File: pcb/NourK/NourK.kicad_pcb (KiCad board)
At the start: 2 copper layers, 218 parts, among them IC1 IS31FL3733B-QFLS4-TR, IC2 IS31FL3733B-QFLS4-TR, J1 SJ-435107RS, J2 USB_C_Receptacle_USB2.0, J3 Conn_ARM_JTAG_SWD_10, J4 SJ-435107RS, J5 USB_C_Receptacle_USB2.0, J6 Conn_ARM_JTAG_SWD_10, SW1 SW_SPST_G, SW10 LAYER, SW11 I, SW12 K, SW13 ,, SW14 LAYER, SW15 O, SW16 L, SW17 ., SW18 LAYER, SW19 P, SW2 SW_SPST_G, SW20 ;, SW21 /, SW22 RCTRL, SW23 [, SW24 ', SW25 RSHIFT, SW26 ], SW27 ENTER, SW28 SW_SPST_G, SW29 SW_SPST_G, SW3 Y, SW30 ESCAPE, SW31 OSKEY, SW32 TAB, SW33 GRAVE, SW34 LEFT_SHIFT, SW35 Q, SW36 A, SW37 Z, SW38 LEFT_CTRL, SW39 W, SW4 H, SW40 S, SW41 X, SW42 LAYER1, SW43 E, SW44 D, SW45 C, SW46 LAYER2, SW47 R, SW48 F, SW49 V, SW5 N, SW50 LEFT_ALT, SW51 T, SW52 G, SW53 B, SW54 SPACE, SW6 SPACE, SW7 U, SW8 J, SW9 M, U1 STM32L082CZYx, U2 AP2112K-3.3, U3 STM32L082CZYx, U4 AP2112K-3.3, Y1 8MHz, Y2 32.768KHz, Y3 8MHz, Y4 32.768KHz

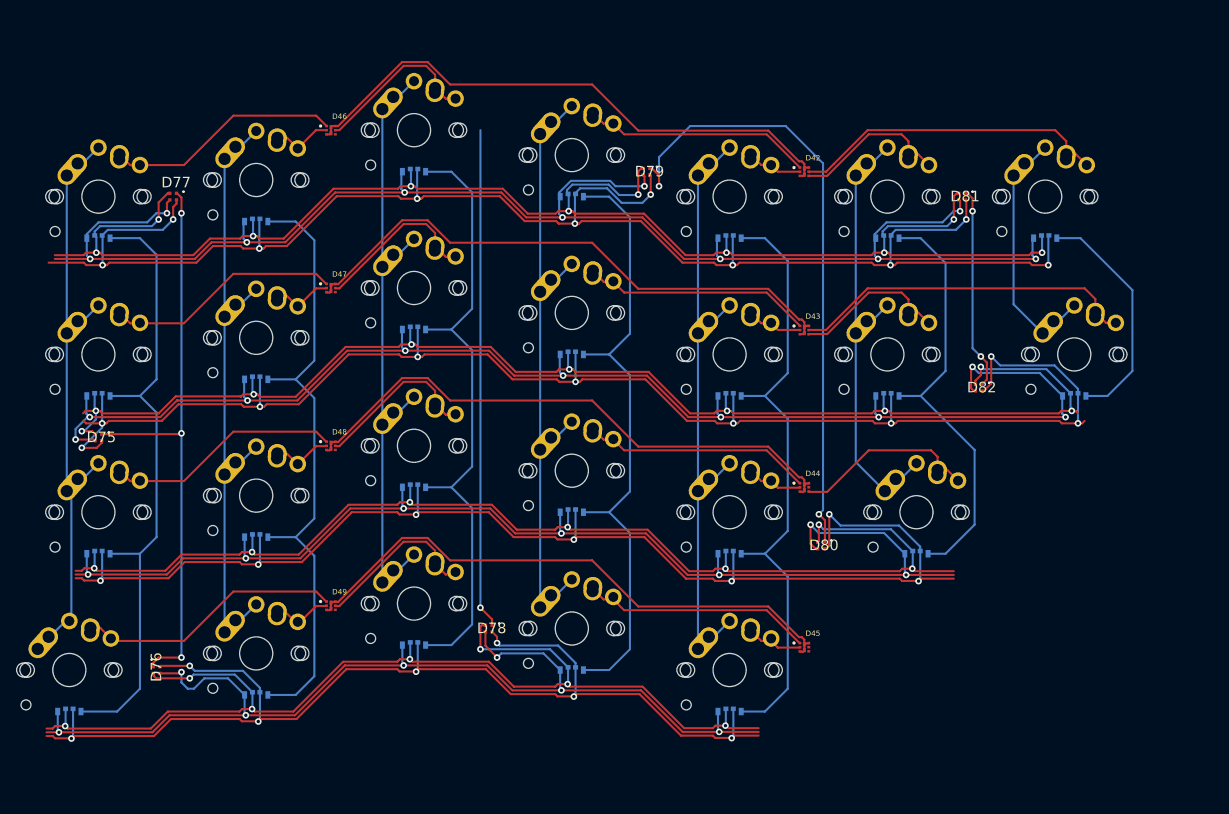
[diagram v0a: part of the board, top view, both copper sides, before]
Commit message: Matrices connection traces
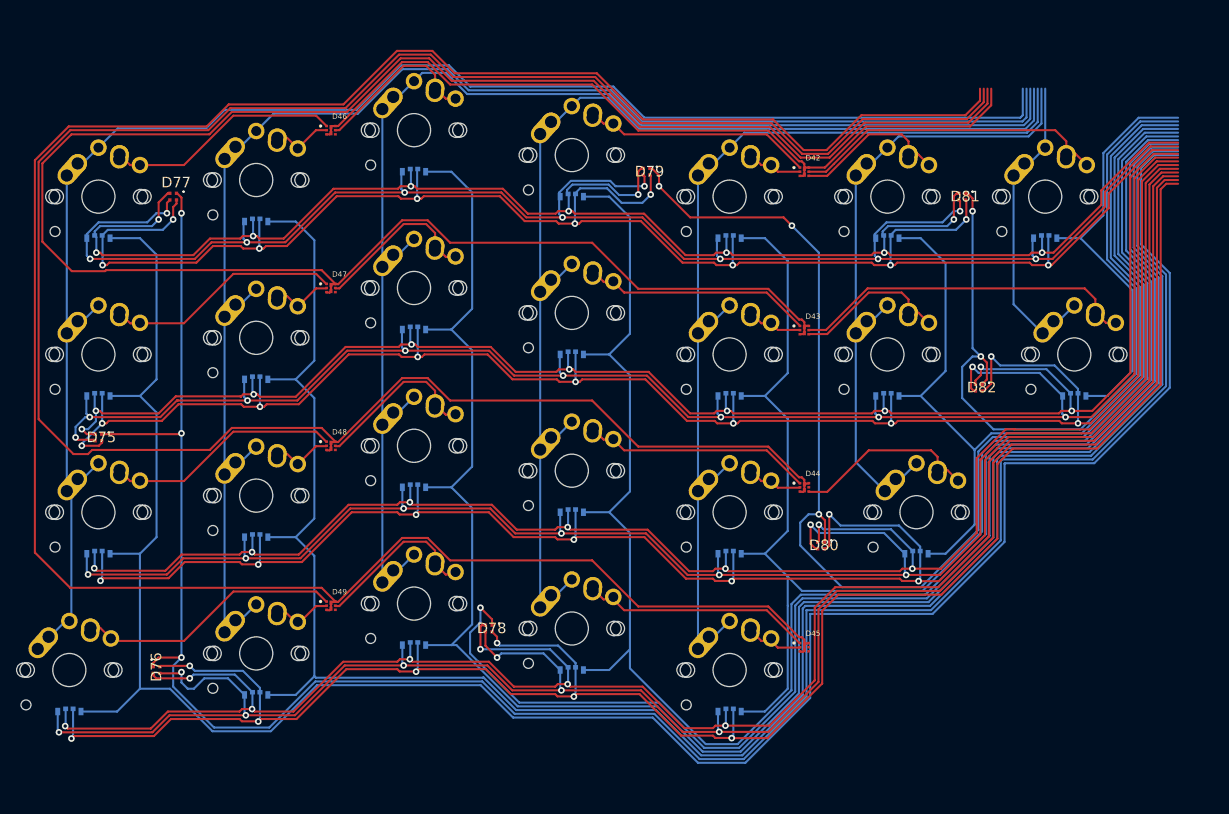
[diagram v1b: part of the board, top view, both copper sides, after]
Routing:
- net /lhs/LHS Core/KEY.ROW4: track 69.1 -> 283.1 mm
- net /lhs/LHS Core/KEY.ROW3: track 69.1 -> 267.8 mm
- net /lhs/LHS Core/LED.CS_COL8: track 70.0 -> 265.5 mm
- net /lhs/LHS Core/LED.CS_COL7: track 76.6 -> 272.0 mm
- net /lhs/LHS Core/KEY.ROW2: track 69.1 -> 244.5 mm
- net /lhs/LHS Core/LED.CS_COL6: track 76.0 -> 246.3 mm
- net /lhs/LHS Core/LED.CS_COL5: track 75.6 -> 230.8 mm
- net /lhs/LHS Core/LED.CS_COL4: track 75.6 -> 210.1 mm
- net /lhs/LHS Core/KEY.COL7: track 68.8 -> 190.1 mm
- net /lhs/LHS Core/KEY.COL6: track 77.8 -> 179.9 mm
- net /lhs/LHS Core/LED.CS_COL9: track 60.2 -> 161.0 mm
- net /lhs/LHS Core/LED.SW_RED4: track 130.7 -> 231.4 mm
- net /lhs/LHS Core/LED.SW_GREEN4: track 132.4 -> 232.0 mm
- net /lhs/LHS Core/LED.SW_BLUE4: track 138.2 -> 237.3 mm
- net /lhs/LHS Core/LED.CS_COL3: track 75.2 -> 171.7 mm
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
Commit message: Initial tracing of the keyboard controller
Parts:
- moved SW29 110.0 mm to (315.7, -18.8)
- moved C36 100.4 mm to (323.4, -2.60), turned to 180 degrees
- moved R24 98.7 mm to (313.8, -13.0)
- moved SW28 90.3 mm to (323.5, 3.25)
- moved R20 87.7 mm to (323.4, 9.00), turned to 180 degrees
- moved J5 80.1 mm to (294.2, -9.75), turned to 180 degrees
- moved Y3 76.2 mm to (301.5, 41.0)
- moved C38 75.4 mm to (306.8, 42.2)
- moved R17 71.7 mm to (301.8, -8.00)
- moved J6 69.0 mm to (313.2, 18.9)
- moved C33 62.9 mm to (292.5, 21.8)
- moved C32 58.3 mm to (289.8, 15.0), turned to -90 degrees
- moved J1 55.8 mm to (237.8, 6.90)
- moved C35 55.1 mm to (286.2, -3.33), turned to 180 degrees
- moved R16 53.3 mm to (301.8, -5.80)
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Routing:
- net GND: track 0.00 -> 83.2 mm, vias 0 -> 10
- net VCC: track 0.00 -> 29.6 mm
- net VBUS: track 0.00 -> 25.7 mm
- net /lhs/LHS Core/~{RST}: track 0.00 -> 11.6 mm
- net Net-(J5-PadB5): track 0.00 -> 9.56 mm, vias 0 -> 2
- net Net-(J5-PadA5): track 0.00 -> 8.99 mm
- net /lhs/LHS Core/BOOT0: track 0.00 -> 8.39 mm
- net Net-(C38-Pad1): track 0.00 -> 4.68 mm
- net Net-(IC2-Pad47): track 0.00 -> 4.46 mm
- net Net-(IC2-Pad46): track 0.00 -> 3.52 mm
- net Net-(IC2-Pad35): track 0.00 -> 3.34 mm
- net /lhs/LHS Core/OSC32_IN: track 0.00 -> 2.91 mm
- net /lhs/LHS Core/OSC32_OUT: track 0.00 -> 2.89 mm
- net /lhs/LHS Core/OSC_IN: track 0.00 -> 2.71 mm
- net +3V3: track 0.00 -> 1.90 mm
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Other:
- copper layers 2 -> 6

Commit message: Re-traced RHS
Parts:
- removed C21, C22, C24, C26: 0.47uF, Capacitor_SMD:C_0805_2012Metric
- removed C23, C25, C27: 0.1uF, Capacitor_SMD:C_0805_2012Metric
- removed C28, C29, C31, C34: 100uF, Capacitor_SMD:C_0805_2012Metric
- removed C30, C33, C35: 1uF, Capacitor_SMD:C_0805_2012Metric
- removed C32: 10uF, Capacitor_SMD:C_0805_2012Metric
- removed C36: 10nF, Capacitor_SMD:C_0805_2012Metric
- removed C37, C38: 10pF, Capacitor_SMD:C_0805_2012Metric
- removed C39, C40: 7pF, Capacitor_SMD:C_0805_2012Metric
- removed FB2: FerriteBead, Resistor_SMD:R_0805_2012Metric
- removed IC2: IS31FL3733B-QFLS4-TR, Nour_KB:QFN40P600X600X80-49N-D
- removed J4: SJ-435107RS, Nour_KB:CUI_SJ-435107RS
- removed J5: USB_C_Receptacle_USB2.0, Nour_KB:GCT_USB4085-GF-A_REVA4
- removed J6: Conn_ARM_JTAG_SWD_10, Connector_PinSocket_1.27mm:PinSocket_2x05_P1.27mm_Vertical
- removed R13, R14, R20, R24: 100K, Resistor_SMD:R_0805_2012Metric
- removed R15: R, Resistor_SMD:R_0805_2012Metric
- removed R16, R17: 5K1, Resistor_SMD:R_0805_2012Metric
- removed R18, R19: 4k7, Resistor_SMD:R_0805_2012Metric
- removed R21, R22: 10K, Resistor_SMD:R_0805_2012Metric
- removed R23: 1990, Resistor_SMD:R_0805_2012Metric
- removed SW28, SW29: SW_SPST_G, Nour_KB:EVQP9102W
- removed Y3: 8MHz, Nour_KB:ECS801830BAGNTR
- removed Y4: 32.768KHz, Nour_KB:ECS327712TR
- added D83: LED_UG_4_2, Nour_KB:LTRBR37G4R4S012502R18, F.Cu at (137.5, 176.0)
- added D84: LED_UG_3_3, Nour_KB:LTRBR37G4R4S012502R18, F.Cu at (137.5, 227.5)
- added U5: NourK_Core, Nour_KB:NourKB_Core, F.Cu at (149.4, 86.4)
- C1, C2, C6: value 0.47uF -> 100uF
- C10: value 1uF -> 7pF
- C11: value 100uF -> 7pF
- C12: value 10uF -> 10pF
- C13: value 1uF -> 10pF
- C14: value 100uF -> 0.47uF
- C15: value 1uF -> 0.47uF
- C16: value 10nF -> 0.1uF
- C17: value 10pF -> 0.47uF
- C18: value 10pF -> 0.1uF
- C19: value 7pF -> 0.47uF
- C20: value 7pF -> 0.1uF
- C3: value 0.1uF -> 100uF
- C4: value 0.47uF -> 10uF
- C5, C7: value 0.1uF -> 1uF
- C8: value 100uF -> 1uF
- C9: value 100uF -> 10nF
- J2: value USB_C_Receptacle_USB2.0 -> Conn_ARM_JTAG_SWD_10; footprint Nour_KB:GCT_USB4085-GF-A_REVA4 -> Connector_PinSocket_1.27mm:PinSocket_2x05_P1.27mm_Vertical
- J3: value Conn_ARM_JTAG_SWD_10 -> USB_C_Receptacle_USB2.0; footprint Connector_PinSocket_1.27mm:PinSocket_2x05_P1.27mm_Vertical -> Nour_KB:GCT_USB4085-GF-A_REVA4
- R1: value 100K -> 10K
- R10, R9: value 10K -> 5K1
- R11: value 1990 -> 100K
- R12: value 100K -> R
- R2: value 100K -> 4k7
- R3: value R -> 4k7
- R4: value 5K1 -> 100K
- R5: value 5K1 -> 10K
- R6: value 4k7 -> 100K
- R7: value 4k7 -> 1990
- U3: value STM32L082CZYx -> NourK_Core; footprint Package_CSP:ST_WLCSP-49_Die447 -> Nour_KB:NourKB_Core_2
- U4: value AP2112K-3.3 -> NourK_Core; footprint Package_TO_SOT_SMD:SOT-23-5 -> Nour_KB:NourKB_Core
- Y1: value 8MHz -> 32.768KHz; footprint Nour_KB:ECS801830BAGNTR -> Nour_KB:ECS327712TR
- Y2: value 32.768KHz -> 8MHz; footprint Nour_KB:ECS327712TR -> Nour_KB:ECS801830BAGNTR
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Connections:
- net /lhs/LHS Core/LED.CS_COL1 renamed /lhs/LHS LEDs/LED.CS_COL1
- net /lhs/LHS Core/LED.CS_COL10 renamed /lhs/LHS LEDs/LED.CS_COL10
- net /lhs/LHS Core/LED.CS_COL11 renamed /lhs/LHS LEDs/LED.CS_COL11
- net /lhs/LHS Core/LED.CS_COL2 renamed /lhs/LHS LEDs/LED.CS_COL2
- net /lhs/LHS Core/LED.CS_COL3 renamed /lhs/LHS LEDs/LED.CS_COL3
- net /lhs/LHS Core/LED.CS_COL4 renamed /lhs/LHS LEDs/LED.CS_COL4
- net /lhs/LHS Core/LED.CS_COL5 renamed /lhs/LHS LEDs/LED.CS_COL5
- net /lhs/LHS Core/LED.CS_COL6 renamed /lhs/LHS LEDs/LED.CS_COL6
- net /lhs/LHS Core/LED.CS_COL7 renamed /lhs/LHS LEDs/LED.CS_COL7
- net /lhs/LHS Core/LED.CS_COL8 renamed /lhs/LHS LEDs/LED.CS_COL8
- net /lhs/LHS Core/LED.SW_BLUE1 renamed /lhs/LHS LEDs/LED.SW_BLUE1
- net /lhs/LHS Core/LED.SW_BLUE2 renamed /lhs/LHS LEDs/LED.SW_BLUE2
- net /lhs/LHS Core/LED.SW_BLUE3 renamed /lhs/LHS LEDs/LED.SW_BLUE3
- net /lhs/LHS Core/LED.SW_BLUE4 renamed /lhs/LHS LEDs/LED.SW_BLUE4
- net /lhs/LHS Core/LED.SW_GREEN1 renamed /lhs/LHS LEDs/LED.SW_GREEN1
- net /lhs/LHS Core/LED.SW_GREEN2 renamed /lhs/LHS LEDs/LED.SW_GREEN2
- net /lhs/LHS Core/LED.SW_GREEN3 renamed /lhs/LHS LEDs/LED.SW_GREEN3
- net /lhs/LHS Core/LED.SW_GREEN4 renamed /lhs/LHS LEDs/LED.SW_GREEN4
- net /lhs/LHS Core/LED.SW_RED1 renamed /lhs/LHS LEDs/LED.SW_RED1
- net /lhs/LHS Core/LED.SW_RED2 renamed /lhs/LHS LEDs/LED.SW_RED2
- net /lhs/LHS Core/LED.SW_RED3 renamed /lhs/LHS LEDs/LED.SW_RED3
- net /lhs/LHS Core/LED.SW_RED4 renamed /lhs/LHS LEDs/LED.SW_RED4
- C10 pad 1: VBUS -> /core/OSC32_IN
- C11 pad 1: VCC -> /core/OSC32_OUT
- C12 pad 1: VCC -> /core/OSC_IN
- C13 pad 1: /rhs/RHS Core/VDDA -> Net-(C13-Pad1)
- C14 pad 1: /rhs/RHS Core/VDDA -> VCC
- C15 pad 1: +3V3 -> VCC
- C16 pad 1: /rhs/RHS Core/~{RST} -> VCC
- C17 pad 1: /rhs/RHS Core/OSC_IN -> VCC
- C18 pad 1: Net-(C18-Pad1) -> VCC
- C19 pad 1: /rhs/RHS Core/OSC32_IN -> VCC
- C20 pad 1: /rhs/RHS Core/OSC32_OUT -> VCC
- C5 pad 1: VCC -> /core/VDDA
- C6 pad 1: VCC -> /core/VDDA
- C7 pad 1: VCC -> VBUS
- C9 pad 1: VCC -> /core/~{RST}
- D1 pad 3: /rhs/RHS Core/KEY.ROW1 -> /rhs/RHS Keys/KEY.ROW10
- D1 pad 6: /rhs/RHS Core/KEY.ROW1 -> /rhs/RHS Keys/KEY.ROW10
- D1 pad 7: /rhs/RHS Core/KEY.ROW1 -> /rhs/RHS Keys/KEY.ROW10
- D1 pad 8: /rhs/RHS Core/KEY.ROW1 -> /rhs/RHS Keys/KEY.ROW10
- D10 pad 1: /rhs/RHS Core/LED.CS_COL1 -> /rhs/RHS LEDs/LED.CS_COL12
- D10 pad 2: /rhs/RHS Core/LED.SW_BLUE2 -> /rhs/RHS LEDs/LED.SW_BLUE3
- D10 pad 3: /rhs/RHS Core/LED.SW_GREEN2 -> /rhs/RHS LEDs/LED.SW_GREEN3
- D10 pad 4: /rhs/RHS Core/LED.SW_RED2 -> /rhs/RHS LEDs/LED.SW_RED3
- D11 pad 1: /rhs/RHS Core/LED.CS_COL1 -> /rhs/RHS LEDs/LED.CS_COL12
- D11 pad 2: /rhs/RHS Core/LED.SW_BLUE3 -> /rhs/RHS LEDs/LED.SW_BLUE2
- D11 pad 3: /rhs/RHS Core/LED.SW_GREEN3 -> /rhs/RHS LEDs/LED.SW_GREEN2
- D11 pad 4: /rhs/RHS Core/LED.SW_RED3 -> /rhs/RHS LEDs/LED.SW_RED2
- D12 pad 1: /rhs/RHS Core/LED.CS_COL1 -> /rhs/RHS LEDs/LED.CS_COL12
- D12 pad 2: /rhs/RHS Core/LED.SW_BLUE4 -> /rhs/RHS LEDs/LED.SW_BLUE1
- D12 pad 3: /rhs/RHS Core/LED.SW_GREEN4 -> /rhs/RHS LEDs/LED.SW_GREEN1
- D12 pad 4: /rhs/RHS Core/LED.SW_RED4 -> /rhs/RHS LEDs/LED.SW_RED1
- D13 pad 1: /rhs/RHS Core/LED.CS_COL2 -> /rhs/RHS LEDs/LED.CS_COL11
- D13 pad 2: /rhs/RHS Core/LED.SW_BLUE1 -> /rhs/RHS LEDs/LED.SW_BLUE4
- D13 pad 3: /rhs/RHS Core/LED.SW_GREEN1 -> /rhs/RHS LEDs/LED.SW_GREEN4
- D13 pad 4: /rhs/RHS Core/LED.SW_RED1 -> /rhs/RHS LEDs/LED.SW_RED4
- D14 pad 1: /rhs/RHS Core/LED.CS_COL2 -> /rhs/RHS LEDs/LED.CS_COL11
- D14 pad 2: /rhs/RHS Core/LED.SW_BLUE2 -> /rhs/RHS LEDs/LED.SW_BLUE3
- D14 pad 3: /rhs/RHS Core/LED.SW_GREEN2 -> /rhs/RHS LEDs/LED.SW_GREEN3
- D14 pad 4: /rhs/RHS Core/LED.SW_RED2 -> /rhs/RHS LEDs/LED.SW_RED3
- D15 pad 1: /rhs/RHS Core/LED.CS_COL2 -> /rhs/RHS LEDs/LED.CS_COL11
- D15 pad 2: /rhs/RHS Core/LED.SW_BLUE3 -> /rhs/RHS LEDs/LED.SW_BLUE2
- D15 pad 3: /rhs/RHS Core/LED.SW_GREEN3 -> /rhs/RHS LEDs/LED.SW_GREEN2
- D15 pad 4: /rhs/RHS Core/LED.SW_RED3 -> /rhs/RHS LEDs/LED.SW_RED2
- D16 pad 1: /rhs/RHS Core/LED.CS_COL2 -> /rhs/RHS LEDs/LED.CS_COL11
- D16 pad 2: /rhs/RHS Core/LED.SW_BLUE4 -> /rhs/RHS LEDs/LED.SW_BLUE1
- D16 pad 3: /rhs/RHS Core/LED.SW_GREEN4 -> /rhs/RHS LEDs/LED.SW_GREEN1
- D16 pad 4: /rhs/RHS Core/LED.SW_RED4 -> /rhs/RHS LEDs/LED.SW_RED1
- D17 pad 1: /rhs/RHS Core/LED.CS_COL3 -> /rhs/RHS LEDs/LED.CS_COL10
- D17 pad 2: /rhs/RHS Core/LED.SW_BLUE1 -> /rhs/RHS LEDs/LED.SW_BLUE4
- D17 pad 3: /rhs/RHS Core/LED.SW_GREEN1 -> /rhs/RHS LEDs/LED.SW_GREEN4
- D17 pad 4: /rhs/RHS Core/LED.SW_RED1 -> /rhs/RHS LEDs/LED.SW_RED4
- D18 pad 1: /rhs/RHS Core/LED.CS_COL3 -> /rhs/RHS LEDs/LED.CS_COL10
- D18 pad 2: /rhs/RHS Core/LED.SW_BLUE2 -> /rhs/RHS LEDs/LED.SW_BLUE3
- D18 pad 3: /rhs/RHS Core/LED.SW_GREEN2 -> /rhs/RHS LEDs/LED.SW_GREEN3
- D18 pad 4: /rhs/RHS Core/LED.SW_RED2 -> /rhs/RHS LEDs/LED.SW_RED3
- D19 pad 1: /rhs/RHS Core/LED.CS_COL3 -> /rhs/RHS LEDs/LED.CS_COL10
- D19 pad 2: /rhs/RHS Core/LED.SW_BLUE3 -> /rhs/RHS LEDs/LED.SW_BLUE2
- D19 pad 3: /rhs/RHS Core/LED.SW_GREEN3 -> /rhs/RHS LEDs/LED.SW_GREEN2
- D19 pad 4: /rhs/RHS Core/LED.SW_RED3 -> /rhs/RHS LEDs/LED.SW_RED2
- D2 pad 3: /rhs/RHS Core/KEY.ROW2 -> /rhs/RHS Keys/KEY.ROW9
- D2 pad 6: /rhs/RHS Core/KEY.ROW2 -> /rhs/RHS Keys/KEY.ROW9
- D2 pad 7: /rhs/RHS Core/KEY.ROW2 -> /rhs/RHS Keys/KEY.ROW9
- D2 pad 8: /rhs/RHS Core/KEY.ROW2 -> /rhs/RHS Keys/KEY.ROW9
- D20 pad 1: /rhs/RHS Core/LED.CS_COL3 -> /rhs/RHS LEDs/LED.CS_COL10
- D20 pad 2: /rhs/RHS Core/LED.SW_BLUE4 -> /rhs/RHS LEDs/LED.SW_BLUE1
- D20 pad 3: /rhs/RHS Core/LED.SW_GREEN4 -> /rhs/RHS LEDs/LED.SW_GREEN1
- D20 pad 4: /rhs/RHS Core/LED.SW_RED4 -> /rhs/RHS LEDs/LED.SW_RED1
- D21 pad 1: /rhs/RHS Core/LED.CS_COL4 -> /rhs/RHS LEDs/LED.CS_COL9
- D21 pad 2: /rhs/RHS Core/LED.SW_BLUE1 -> /rhs/RHS LEDs/LED.SW_BLUE4
- D21 pad 3: /rhs/RHS Core/LED.SW_GREEN1 -> /rhs/RHS LEDs/LED.SW_GREEN4
- D21 pad 4: /rhs/RHS Core/LED.SW_RED1 -> /rhs/RHS LEDs/LED.SW_RED4
- D22 pad 1: /rhs/RHS Core/LED.CS_COL4 -> /rhs/RHS LEDs/LED.CS_COL9
- D22 pad 2: /rhs/RHS Core/LED.SW_BLUE2 -> /rhs/RHS LEDs/LED.SW_BLUE3
- D22 pad 3: /rhs/RHS Core/LED.SW_GREEN2 -> /rhs/RHS LEDs/LED.SW_GREEN3
- D22 pad 4: /rhs/RHS Core/LED.SW_RED2 -> /rhs/RHS LEDs/LED.SW_RED3
- D23 pad 1: /rhs/RHS Core/LED.CS_COL4 -> /rhs/RHS LEDs/LED.CS_COL9
- D23 pad 2: /rhs/RHS Core/LED.SW_BLUE3 -> /rhs/RHS LEDs/LED.SW_BLUE2
- D23 pad 3: /rhs/RHS Core/LED.SW_GREEN3 -> /rhs/RHS LEDs/LED.SW_GREEN2
- D23 pad 4: /rhs/RHS Core/LED.SW_RED3 -> /rhs/RHS LEDs/LED.SW_RED2
- D24 pad 1: /rhs/RHS Core/LED.CS_COL4 -> /rhs/RHS LEDs/LED.CS_COL9
- D24 pad 2: /rhs/RHS Core/LED.SW_BLUE4 -> /rhs/RHS LEDs/LED.SW_BLUE1
- D24 pad 3: /rhs/RHS Core/LED.SW_GREEN4 -> /rhs/RHS LEDs/LED.SW_GREEN1
- D24 pad 4: /rhs/RHS Core/LED.SW_RED4 -> /rhs/RHS LEDs/LED.SW_RED1
- D25 pad 1: /rhs/RHS Core/LED.CS_COL5 -> /rhs/RHS LEDs/LED.CS_COL8
- D25 pad 2: /rhs/RHS Core/LED.SW_BLUE1 -> /rhs/RHS LEDs/LED.SW_BLUE4
- D25 pad 3: /rhs/RHS Core/LED.SW_GREEN1 -> /rhs/RHS LEDs/LED.SW_GREEN4
- D25 pad 4: /rhs/RHS Core/LED.SW_RED1 -> /rhs/RHS LEDs/LED.SW_RED4
- D26 pad 1: /rhs/RHS Core/LED.CS_COL5 -> /rhs/RHS LEDs/LED.CS_COL8
- D26 pad 2: /rhs/RHS Core/LED.SW_BLUE2 -> /rhs/RHS LEDs/LED.SW_BLUE3
- D26 pad 3: /rhs/RHS Core/LED.SW_GREEN2 -> /rhs/RHS LEDs/LED.SW_GREEN3
- D26 pad 4: /rhs/RHS Core/LED.SW_RED2 -> /rhs/RHS LEDs/LED.SW_RED3
- D27 pad 1: /rhs/RHS Core/LED.CS_COL5 -> /rhs/RHS LEDs/LED.CS_COL8
- D27 pad 2: /rhs/RHS Core/LED.SW_BLUE3 -> /rhs/RHS LEDs/LED.SW_BLUE2
- D27 pad 3: /rhs/RHS Core/LED.SW_GREEN3 -> /rhs/RHS LEDs/LED.SW_GREEN2
- D27 pad 4: /rhs/RHS Core/LED.SW_RED3 -> /rhs/RHS LEDs/LED.SW_RED2
- D28 pad 1: /rhs/RHS Core/LED.CS_COL5 -> /rhs/RHS LEDs/LED.CS_COL8
- D28 pad 2: /rhs/RHS Core/LED.SW_BLUE4 -> /rhs/RHS LEDs/LED.SW_BLUE1
- D28 pad 3: /rhs/RHS Core/LED.SW_GREEN4 -> /rhs/RHS LEDs/LED.SW_GREEN1
- D28 pad 4: /rhs/RHS Core/LED.SW_RED4 -> /rhs/RHS LEDs/LED.SW_RED1
- D29 pad 1: /rhs/RHS Core/LED.CS_COL6 -> /rhs/RHS LEDs/LED.CS_COL7
- D29 pad 2: /rhs/RHS Core/LED.SW_BLUE1 -> /rhs/RHS LEDs/LED.SW_BLUE4
- D29 pad 3: /rhs/RHS Core/LED.SW_GREEN1 -> /rhs/RHS LEDs/LED.SW_GREEN4
- D29 pad 4: /rhs/RHS Core/LED.SW_RED1 -> /rhs/RHS LEDs/LED.SW_RED4
- D3 pad 3: /rhs/RHS Core/KEY.ROW3 -> /rhs/RHS Keys/KEY.ROW2
- D3 pad 6: /rhs/RHS Core/KEY.ROW3 -> /rhs/RHS Keys/KEY.ROW2
- D3 pad 7: /rhs/RHS Core/KEY.ROW3 -> /rhs/RHS Keys/KEY.ROW2
- D3 pad 8: /rhs/RHS Core/KEY.ROW3 -> /rhs/RHS Keys/KEY.ROW2
- D30 pad 1: /rhs/RHS Core/LED.CS_COL6 -> /rhs/RHS LEDs/LED.CS_COL7
- D30 pad 2: /rhs/RHS Core/LED.SW_BLUE2 -> /rhs/RHS LEDs/LED.SW_BLUE3
- D30 pad 3: /rhs/RHS Core/LED.SW_GREEN2 -> /rhs/RHS LEDs/LED.SW_GREEN3
- D30 pad 4: /rhs/RHS Core/LED.SW_RED2 -> /rhs/RHS LEDs/LED.SW_RED3
- D31 pad 1: /rhs/RHS Core/LED.CS_COL6 -> /rhs/RHS LEDs/LED.CS_COL7
- D31 pad 2: /rhs/RHS Core/LED.SW_BLUE3 -> /rhs/RHS LEDs/LED.SW_BLUE2
- D31 pad 3: /rhs/RHS Core/LED.SW_GREEN3 -> /rhs/RHS LEDs/LED.SW_GREEN2
- D31 pad 4: /rhs/RHS Core/LED.SW_RED3 -> /rhs/RHS LEDs/LED.SW_RED2
- D32 pad 1: /rhs/RHS Core/LED.CS_COL7 -> /rhs/RHS LEDs/LED.CS_COL6
- D32 pad 2: /rhs/RHS Core/LED.SW_BLUE1 -> /rhs/RHS LEDs/LED.SW_BLUE4
- D32 pad 3: /rhs/RHS Core/LED.SW_GREEN1 -> /rhs/RHS LEDs/LED.SW_GREEN4
- D32 pad 4: /rhs/RHS Core/LED.SW_RED1 -> /rhs/RHS LEDs/LED.SW_RED4
- D33 pad 1: /rhs/RHS Core/LED.CS_COL7 -> /rhs/RHS LEDs/LED.CS_COL6
- D33 pad 2: /rhs/RHS Core/LED.SW_BLUE2 -> /rhs/RHS LEDs/LED.SW_BLUE3
- D33 pad 3: /rhs/RHS Core/LED.SW_GREEN2 -> /rhs/RHS LEDs/LED.SW_GREEN3
- D33 pad 4: /rhs/RHS Core/LED.SW_RED2 -> /rhs/RHS LEDs/LED.SW_RED3
- D34 pad 1: /rhs/RHS Core/LED.CS_COL8 -> /rhs/RHS LEDs/LED.CS_COL16
- D34 pad 2: /rhs/RHS Core/LED.SW_RED1 -> /rhs/RHS LEDs/LED.SW_RED3
- D34 pad 3: /rhs/RHS Core/LED.SW_BLUE1 -> /rhs/RHS LEDs/LED.SW_BLUE3
- D34 pad 4: /rhs/RHS Core/LED.SW_GREEN1 -> /rhs/RHS LEDs/LED.SW_GREEN3
- D35 pad 1: /rhs/RHS Core/LED.CS_COL8 -> /rhs/RHS LEDs/LED.CS_COL16
- D35 pad 2: /rhs/RHS Core/LED.SW_RED2 -> /rhs/RHS LEDs/LED.SW_RED1
- D35 pad 3: /rhs/RHS Core/LED.SW_BLUE2 -> /rhs/RHS LEDs/LED.SW_BLUE1
- D35 pad 4: /rhs/RHS Core/LED.SW_GREEN2 -> /rhs/RHS LEDs/LED.SW_GREEN1
- D36 pad 1: /rhs/RHS Core/LED.CS_COL8 -> /rhs/RHS LEDs/LED.CS_COL14
- D36 pad 2: /rhs/RHS Core/LED.SW_RED3 -> /rhs/RHS LEDs/LED.SW_RED1
- D36 pad 3: /rhs/RHS Core/LED.SW_BLUE3 -> /rhs/RHS LEDs/LED.SW_BLUE1
- D36 pad 4: /rhs/RHS Core/LED.SW_GREEN3 -> /rhs/RHS LEDs/LED.SW_GREEN1
- D37 pad 1: /rhs/RHS Core/LED.CS_COL8 -> /rhs/RHS LEDs/LED.CS_COL13
- D37 pad 2: /rhs/RHS Core/LED.SW_RED4 -> /rhs/RHS LEDs/LED.SW_RED2
- D37 pad 3: /rhs/RHS Core/LED.SW_BLUE4 -> /rhs/RHS LEDs/LED.SW_BLUE2
- D37 pad 4: /rhs/RHS Core/LED.SW_GREEN4 -> /rhs/RHS LEDs/LED.SW_GREEN2
- D38 pad 1: /rhs/RHS Core/LED.CS_COL9 -> /rhs/RHS LEDs/LED.CS_COL16
- D38 pad 2: /rhs/RHS Core/LED.SW_RED1 -> /rhs/RHS LEDs/LED.SW_RED4
- D38 pad 3: /rhs/RHS Core/LED.SW_BLUE1 -> /rhs/RHS LEDs/LED.SW_BLUE4
- D38 pad 4: /rhs/RHS Core/LED.SW_GREEN1 -> /rhs/RHS LEDs/LED.SW_GREEN4
- D39 pad 1: /rhs/RHS Core/LED.CS_COL9 -> /rhs/RHS LEDs/LED.CS_COL14
- D39 pad 2: /rhs/RHS Core/LED.SW_RED2 -> /rhs/RHS LEDs/LED.SW_RED4
- D39 pad 3: /rhs/RHS Core/LED.SW_BLUE2 -> /rhs/RHS LEDs/LED.SW_BLUE4
- D39 pad 4: /rhs/RHS Core/LED.SW_GREEN2 -> /rhs/RHS LEDs/LED.SW_GREEN4
- D4 pad 3: /rhs/RHS Core/KEY.ROW4 -> /rhs/RHS Keys/KEY.ROW1
- D4 pad 6: /rhs/RHS Core/KEY.ROW4 -> /rhs/RHS Keys/KEY.ROW1
- D4 pad 7: /rhs/RHS Core/KEY.ROW4 -> /rhs/RHS Keys/KEY.ROW1
- D4 pad 8: /rhs/RHS Core/KEY.ROW4 -> /rhs/RHS Keys/KEY.ROW1
- D40 pad 1: /rhs/RHS Core/LED.CS_COL9 -> /rhs/RHS LEDs/LED.CS_COL13
- D40 pad 2: /rhs/RHS Core/LED.SW_RED3 -> /rhs/RHS LEDs/LED.SW_RED4
- D40 pad 3: /rhs/RHS Core/LED.SW_BLUE3 -> /rhs/RHS LEDs/LED.SW_BLUE4
- D40 pad 4: /rhs/RHS Core/LED.SW_GREEN3 -> /rhs/RHS LEDs/LED.SW_GREEN4
- D41 pad 1: /rhs/RHS Core/LED.CS_COL9 -> /rhs/RHS LEDs/LED.CS_COL13
- D41 pad 2: /rhs/RHS Core/LED.SW_RED4 -> /rhs/RHS LEDs/LED.SW_RED3
- D41 pad 3: /rhs/RHS Core/LED.SW_BLUE4 -> /rhs/RHS LEDs/LED.SW_BLUE3
- D41 pad 4: /rhs/RHS Core/LED.SW_GREEN4 -> /rhs/RHS LEDs/LED.SW_GREEN3
- D42 pad 3: /lhs/LHS Core/KEY.ROW1 -> /lhs/LHS Keys/KEY.ROW1
- D42 pad 6: /lhs/LHS Core/KEY.ROW1 -> /lhs/LHS Keys/KEY.ROW1
- D42 pad 7: /lhs/LHS Core/KEY.ROW1 -> /lhs/LHS Keys/KEY.ROW1
- D42 pad 8: /lhs/LHS Core/KEY.ROW1 -> /lhs/LHS Keys/KEY.ROW1
- D43 pad 3: /lhs/LHS Core/KEY.ROW2 -> /lhs/LHS Keys/KEY.ROW2
- D43 pad 6: /lhs/LHS Core/KEY.ROW2 -> /lhs/LHS Keys/KEY.ROW2
- D43 pad 7: /lhs/LHS Core/KEY.ROW2 -> /lhs/LHS Keys/KEY.ROW2
- D43 pad 8: /lhs/LHS Core/KEY.ROW2 -> /lhs/LHS Keys/KEY.ROW2
- D44 pad 3: /lhs/LHS Core/KEY.ROW3 -> /lhs/LHS Keys/KEY.ROW3
- D44 pad 6: /lhs/LHS Core/KEY.ROW3 -> /lhs/LHS Keys/KEY.ROW3
- D44 pad 7: /lhs/LHS Core/KEY.ROW3 -> /lhs/LHS Keys/KEY.ROW3
- D44 pad 8: /lhs/LHS Core/KEY.ROW3 -> /lhs/LHS Keys/KEY.ROW3
- D45 pad 3: /lhs/LHS Core/KEY.ROW4 -> /lhs/LHS Keys/KEY.ROW4
- D45 pad 6: /lhs/LHS Core/KEY.ROW4 -> /lhs/LHS Keys/KEY.ROW4
- D45 pad 7: /lhs/LHS Core/KEY.ROW4 -> /lhs/LHS Keys/KEY.ROW4
- D45 pad 8: /lhs/LHS Core/KEY.ROW4 -> /lhs/LHS Keys/KEY.ROW4
- D46 pad 3: /lhs/LHS Core/KEY.ROW1 -> /lhs/LHS Keys/KEY.ROW1
- D46 pad 6: /lhs/LHS Core/KEY.ROW1 -> /lhs/LHS Keys/KEY.ROW1
- D46 pad 7: /lhs/LHS Core/KEY.ROW1 -> /lhs/LHS Keys/KEY.ROW1
- D46 pad 8: /lhs/LHS Core/KEY.ROW1 -> /lhs/LHS Keys/KEY.ROW1
- D47 pad 3: /lhs/LHS Core/KEY.ROW2 -> /lhs/LHS Keys/KEY.ROW2
- D47 pad 6: /lhs/LHS Core/KEY.ROW2 -> /lhs/LHS Keys/KEY.ROW2
- D47 pad 7: /lhs/LHS Core/KEY.ROW2 -> /lhs/LHS Keys/KEY.ROW2
- D47 pad 8: /lhs/LHS Core/KEY.ROW2 -> /lhs/LHS Keys/KEY.ROW2
- D48 pad 3: /lhs/LHS Core/KEY.ROW3 -> /lhs/LHS Keys/KEY.ROW3
- D48 pad 6: /lhs/LHS Core/KEY.ROW3 -> /lhs/LHS Keys/KEY.ROW3
- D48 pad 7: /lhs/LHS Core/KEY.ROW3 -> /lhs/LHS Keys/KEY.ROW3
- D48 pad 8: /lhs/LHS Core/KEY.ROW3 -> /lhs/LHS Keys/KEY.ROW3
- D49 pad 3: /lhs/LHS Core/KEY.ROW4 -> /lhs/LHS Keys/KEY.ROW4
- D49 pad 6: /lhs/LHS Core/KEY.ROW4 -> /lhs/LHS Keys/KEY.ROW4
- D49 pad 7: /lhs/LHS Core/KEY.ROW4 -> /lhs/LHS Keys/KEY.ROW4
- D49 pad 8: /lhs/LHS Core/KEY.ROW4 -> /lhs/LHS Keys/KEY.ROW4
- D5 pad 3: /rhs/RHS Core/KEY.ROW1 -> /rhs/RHS Keys/KEY.ROW10
- D5 pad 6: /rhs/RHS Core/KEY.ROW1 -> /rhs/RHS Keys/KEY.ROW10
- D5 pad 7: /rhs/RHS Core/KEY.ROW1 -> /rhs/RHS Keys/KEY.ROW10
- D5 pad 8: /rhs/RHS Core/KEY.ROW1 -> /rhs/RHS Keys/KEY.ROW10
- D6 pad 3: /rhs/RHS Core/KEY.ROW2 -> /rhs/RHS Keys/KEY.ROW9
- D6 pad 6: /rhs/RHS Core/KEY.ROW2 -> /rhs/RHS Keys/KEY.ROW9
- D6 pad 7: /rhs/RHS Core/KEY.ROW2 -> /rhs/RHS Keys/KEY.ROW9
- D6 pad 8: /rhs/RHS Core/KEY.ROW2 -> /rhs/RHS Keys/KEY.ROW9
- D7 pad 3: /rhs/RHS Core/KEY.ROW3 -> /rhs/RHS Keys/KEY.ROW2
- D7 pad 6: /rhs/RHS Core/KEY.ROW3 -> /rhs/RHS Keys/KEY.ROW2
- D7 pad 7: /rhs/RHS Core/KEY.ROW3 -> /rhs/RHS Keys/KEY.ROW2
- D7 pad 8: /rhs/RHS Core/KEY.ROW3 -> /rhs/RHS Keys/KEY.ROW2
- D78 pad 1: /lhs/LHS Core/LED.CS_COL9 -> /lhs/LHS LEDs/LED.CS_COL9
- D8 pad 3: /rhs/RHS Core/KEY.ROW4 -> /rhs/RHS Keys/KEY.ROW1
- D8 pad 6: /rhs/RHS Core/KEY.ROW4 -> /rhs/RHS Keys/KEY.ROW1
- D8 pad 7: /rhs/RHS Core/KEY.ROW4 -> /rhs/RHS Keys/KEY.ROW1
- D8 pad 8: /rhs/RHS Core/KEY.ROW4 -> /rhs/RHS Keys/KEY.ROW1
- D9 pad 1: /rhs/RHS Core/LED.CS_COL1 -> /rhs/RHS LEDs/LED.CS_COL12
- D9 pad 2: /rhs/RHS Core/LED.SW_BLUE1 -> /rhs/RHS LEDs/LED.SW_BLUE4
- D9 pad 3: /rhs/RHS Core/LED.SW_GREEN1 -> /rhs/RHS LEDs/LED.SW_GREEN4
- D9 pad 4: /rhs/RHS Core/LED.SW_RED1 -> /rhs/RHS LEDs/LED.SW_RED4
- FB1 pad 2: /rhs/RHS Core/VDDA -> /core/VDDA
- IC1 pad 10: /rhs/RHS Core/LED.SW_RED2 -> /core/LED.SW_RED2
- IC1 pad 11: /rhs/RHS Core/LED.SW_BLUE2 -> /core/LED.SW_BLUE2
- IC1 pad 13: /rhs/RHS Core/LED.SW_GREEN1 -> /core/LED.SW_GREEN1
- IC1 pad 14: /rhs/RHS Core/LED.SW_RED1 -> /core/LED.SW_RED1
- IC1 pad 15: /rhs/RHS Core/LED.SW_BLUE1 -> /core/LED.SW_BLUE1
- IC1 pad 16: /rhs/RHS Core/LED.CS_COL1 -> /core/LED.CS_COL1
- IC1 pad 17: /rhs/RHS Core/LED.CS_COL2 -> /core/LED.CS_COL2
- IC1 pad 18: /rhs/RHS Core/LED.CS_COL3 -> /core/LED.CS_COL3
- IC1 pad 19: /rhs/RHS Core/LED.CS_COL4 -> /core/LED.CS_COL4
- IC1 pad 2: /rhs/RHS Core/LED.SW_GREEN4 -> /core/LED.SW_GREEN4
- IC1 pad 21: /rhs/RHS Core/LED.CS_COL5 -> /core/LED.CS_COL5
- IC1 pad 22: /rhs/RHS Core/LED.CS_COL6 -> /core/LED.CS_COL6
- IC1 pad 23: /rhs/RHS Core/LED.CS_COL7 -> /core/LED.CS_COL7
- IC1 pad 24: /rhs/RHS Core/LED.CS_COL8 -> /core/LED.CS_COL8
- IC1 pad 25: /rhs/RHS Core/LED.CS_COL9 -> /core/LED.CS_COL9
- IC1 pad 26: /rhs/RHS Core/LED.CS_COL10 -> /core/LED.CS_COL10
- IC1 pad 27: /rhs/RHS Core/LED.CS_COL11 -> /core/LED.CS_COL11
- IC1 pad 28: /rhs/RHS Core/LED.CS_COL12 -> /core/LED.CS_COL12
- IC1 pad 3: /rhs/RHS Core/LED.SW_RED4 -> /core/LED.SW_RED4
- IC1 pad 30: /rhs/RHS Core/LED.CS_COL13 -> /core/LED.CS_COL13
- IC1 pad 31: /rhs/RHS Core/LED.CS_COL14 -> /core/LED.CS_COL14
- IC1 pad 32: /rhs/RHS Core/LED.CS_COL15 -> /core/LED.CS_COL15
- IC1 pad 33: /rhs/RHS Core/LED.CS_COL16 -> /core/LED.CS_COL16
- IC1 pad 4: /rhs/RHS Core/LED.SW_BLUE4 -> /core/LED.SW_BLUE4
- IC1 pad 41: /rhs/RHS Core/I2C_SDA -> /core/I2C_SDA
- IC1 pad 42: /rhs/RHS Core/I2C_SCL -> /core/I2C_SCL
- IC1 pad 6: /rhs/RHS Core/LED.SW_GREEN3 -> /core/LED.SW_GREEN3
- IC1 pad 7: /rhs/RHS Core/LED.SW_RED3 -> /core/LED.SW_RED3
- IC1 pad 8: /rhs/RHS Core/LED.SW_BLUE3 -> /core/LED.SW_BLUE3
- IC1 pad 9: /rhs/RHS Core/LED.SW_GREEN2 -> /core/LED.SW_GREEN2
- J1 pad 3: /lhs/USART.RX -> /core/USART.RX
- J1 pad 4: /lhs/USART.TX -> /core/USART.TX
- R1 pad 2: Net-(IC1-Pad46) -> /core/VREF+
- R10 pad 1: /rhs/RHS Core/VREF+ -> Net-(J3-PadB5)
- R11 pad 1: /rhs/RHS Core/OSC_OUT -> Net-(IC1-Pad47)
- R11 pad 2: Net-(C18-Pad1) -> GND
- R12 pad 1: GND -> Net-(IC1-Pad35)
- R12 pad 2: /rhs/RHS Core/BOOT0 -> GND
- R2 pad 1: Net-(IC1-Pad47) -> /core/I2C_SCL
- R2 pad 2: GND -> VCC
- R3 pad 1: Net-(IC1-Pad35) -> VCC
- R3 pad 2: GND -> /core/I2C_SDA
- R4 pad 1: Net-(J2-PadA5) -> GND
- R4 pad 2: GND -> /core/BOOT0
- R5 pad 1: Net-(J2-PadB5) -> /core/VREF+
- R6 pad 1: /rhs/RHS Core/I2C_SCL -> /core/~{RST}
- R7 pad 1: VCC -> /core/OSC_OUT
- R7 pad 2: /rhs/RHS Core/I2C_SDA -> Net-(C13-Pad1)
- R8 pad 1: /rhs/RHS Core/~{RST} -> VCC
- R8 pad 2: VCC -> Net-(IC1-Pad46)
- R9 pad 1: VCC -> Net-(J3-PadA5)
- R9 pad 2: /rhs/RHS Core/VREF+ -> GND
- SW1 pad 1: GND -> /core/BOOT0
- SW1 pad 2: /rhs/RHS Core/~{RST} -> VCC
- SW1 pad 3: GND -> /core/BOOT0
- SW1 pad 4: /rhs/RHS Core/~{RST} -> VCC
- SW10 pad 2: /rhs/RHS Core/KEY.COL2 -> /rhs/RHS Keys/KEY.COL1
- SW11 pad 2: /rhs/RHS Core/KEY.COL3 -> /rhs/RHS Keys/KEY.COL6
- SW12 pad 2: /rhs/RHS Core/KEY.COL3 -> /rhs/RHS Keys/KEY.COL6
- SW13 pad 2: /rhs/RHS Core/KEY.COL3 -> /rhs/RHS Keys/KEY.COL6
- SW14 pad 2: /rhs/RHS Core/KEY.COL3 -> /rhs/RHS Keys/KEY.COL6
- SW15 pad 2: /rhs/RHS Core/KEY.COL4 -> /rhs/RHS Keys/KEY.COL7
- SW16 pad 2: /rhs/RHS Core/KEY.COL4 -> /rhs/RHS Keys/KEY.COL7
- SW17 pad 2: /rhs/RHS Core/KEY.COL4 -> /rhs/RHS Keys/KEY.COL7
- SW18 pad 2: /rhs/RHS Core/KEY.COL4 -> /rhs/RHS Keys/KEY.COL7
- SW19 pad 2: /rhs/RHS Core/KEY.COL5 -> /rhs/RHS Keys/KEY.COL8
- SW2 pad 1: /rhs/RHS Core/BOOT0 -> GND
- SW2 pad 2: VCC -> /core/~{RST}
- SW2 pad 3: /rhs/RHS Core/BOOT0 -> GND
- SW2 pad 4: VCC -> /core/~{RST}
- SW20 pad 2: /rhs/RHS Core/KEY.COL5 -> /rhs/RHS Keys/KEY.COL8
- SW21 pad 2: /rhs/RHS Core/KEY.COL5 -> /rhs/RHS Keys/KEY.COL8
- SW22 pad 2: /rhs/RHS Core/KEY.COL5 -> /rhs/RHS Keys/KEY.COL8
- SW23 pad 2: /rhs/RHS Core/KEY.COL6 -> /rhs/RHS Keys/KEY.COL9
- SW24 pad 2: /rhs/RHS Core/KEY.COL6 -> /rhs/RHS Keys/KEY.COL9
- SW25 pad 2: /rhs/RHS Core/KEY.COL6 -> /rhs/RHS Keys/KEY.COL9
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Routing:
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- added copper zone on B.Cu, net GND
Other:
- board outline added: 156.2 x 227.5 mm
- copper layers 6 -> 4

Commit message: Initial RHS DRC checked
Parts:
- U1: footprint Package_CSP:ST_WLCSP-49_Die447 -> Nour_KB:ST_WLCSP-49_Die447
- moved D8 2.00 mm to (82.0, 232.0)
- moved C8 1.59 mm to (132.2, -38.5)
- moved R9 0.36 mm to (113.6, 27.5)
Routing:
- net /rhs/RHS LEDs/LED.CS_COL6: track 191.0 -> 170.4 mm, vias 2 -> 1
- net /rhs/RHS LEDs/LED.CS_COL13: track 201.5 -> 189.7 mm
- net /rhs/RHS LEDs/LED.CS_COL7: track 173.4 -> 167.0 mm
- net /rhs/RHS LEDs/LED.SW_RED3: track 202.1 -> 196.2 mm
- net /rhs/RHS LEDs/LED.SW_GREEN3: track 205.2 -> 200.7 mm
- net Net-(D43-Pad4): track 16.7 -> 20.3 mm
- net /rhs/RHS LEDs/LED.SW_BLUE3: track 193.5 -> 190.7 mm
- net Net-(D8-Pad5): track 40.2 -> 38.1 mm
- net Net-(D8-Pad4): track 18.9 -> 16.8 mm
- net /rhs/RHS Keys/KEY.ROW1: track 116.7 -> 114.7 mm
- net /lhs/LHS Keys/KEY.COL6: track 153.3 -> 151.8 mm
- net /rhs/RHS LEDs/LED.CS_COL10: track 130.0 -> 129.6 mm, vias 2 -> 1
- net /rhs/RHS LEDs/LED.CS_COL15: vias 4 -> 3

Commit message: RHS and LHS wire complete and initial DRC
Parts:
- added D85: LED_UG_1_2, Nour_KB:LTRBR37G4R4S012502R18, F.Cu at (52.5, 171.0)
- added D86: LED_UG_2_3, Nour_KB:LTRBR37G4R4S012502R18, F.Cu at (90.5, 225.0)
- SW10, SW11, SW12, SW13, SW14, SW15, SW16, SW17, SW18, SW19, SW20, SW21, SW22, SW23, SW24, SW25, SW26, SW27, SW3, SW30, SW31, SW32, SW33, SW34, SW35, SW36, SW37, SW38, SW39, SW4, SW40, SW41, SW42, SW43, SW44, SW45, SW46, SW47, SW48, SW49, SW5, SW50, SW51, SW52, SW53, SW54, SW6, SW7, SW8, SW9: footprint Keebio-Parts:MX-Alps-Choc-1U-NoLED -> Nour_KB:MX_Choc_1U
- U4, U5: footprint Nour_KB:NourKB_Core -> Nour_KB:NourKB_Core_2
- moved D13 190.1 mm to (-43.0, 175.5)
- moved D17 190.1 mm to (-62.0, 169.5)
- moved D21 190.1 mm to (-81.0, 172.5)
- moved D25 190.1 mm to (-100.0, 177.5)
- moved D29 190.1 mm to (-119.0, 177.5)
- moved D32 190.1 mm to (-138.0, 177.5)
- moved D9 190.1 mm to (-24.0, 177.5)
- moved D10 190.1 mm to (-24.0, 196.5)
- moved D11 190.1 mm to (-24.0, 215.5)
- moved D12 190.1 mm to (-20.5, 234.5)
- moved D14 190.1 mm to (-43.0, 194.5)
- moved D15 190.1 mm to (-43.0, 213.5)
- moved D16 190.1 mm to (-43.0, 232.5)
- moved D18 190.1 mm to (-62.0, 188.5)
- moved D19 190.1 mm to (-62.0, 207.5)
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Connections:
- D3 pad 3: /rhs/RHS Keys/KEY.ROW2 -> /rhs/RHS Keys/KEY.ROW4
- D3 pad 6: /rhs/RHS Keys/KEY.ROW2 -> /rhs/RHS Keys/KEY.ROW4
- D3 pad 7: /rhs/RHS Keys/KEY.ROW2 -> /rhs/RHS Keys/KEY.ROW4
- D3 pad 8: /rhs/RHS Keys/KEY.ROW2 -> /rhs/RHS Keys/KEY.ROW4
- D4 pad 3: /rhs/RHS Keys/KEY.ROW1 -> /rhs/RHS Keys/KEY.ROW3
- D4 pad 6: /rhs/RHS Keys/KEY.ROW1 -> /rhs/RHS Keys/KEY.ROW3
- D4 pad 7: /rhs/RHS Keys/KEY.ROW1 -> /rhs/RHS Keys/KEY.ROW3
- D4 pad 8: /rhs/RHS Keys/KEY.ROW1 -> /rhs/RHS Keys/KEY.ROW3
- D44 pad 3: /lhs/LHS Keys/KEY.ROW3 -> /lhs/LHS Keys/KEY.ROW9
- D44 pad 6: /lhs/LHS Keys/KEY.ROW3 -> /lhs/LHS Keys/KEY.ROW9
- D44 pad 7: /lhs/LHS Keys/KEY.ROW3 -> /lhs/LHS Keys/KEY.ROW9
- D44 pad 8: /lhs/LHS Keys/KEY.ROW3 -> /lhs/LHS Keys/KEY.ROW9
- D45 pad 3: /lhs/LHS Keys/KEY.ROW4 -> /lhs/LHS Keys/KEY.ROW10
- D45 pad 6: /lhs/LHS Keys/KEY.ROW4 -> /lhs/LHS Keys/KEY.ROW10
- D45 pad 7: /lhs/LHS Keys/KEY.ROW4 -> /lhs/LHS Keys/KEY.ROW10
- D45 pad 8: /lhs/LHS Keys/KEY.ROW4 -> /lhs/LHS Keys/KEY.ROW10
- D48 pad 3: /lhs/LHS Keys/KEY.ROW3 -> /lhs/LHS Keys/KEY.ROW9
- D48 pad 6: /lhs/LHS Keys/KEY.ROW3 -> /lhs/LHS Keys/KEY.ROW9
- D48 pad 7: /lhs/LHS Keys/KEY.ROW3 -> /lhs/LHS Keys/KEY.ROW9
- D48 pad 8: /lhs/LHS Keys/KEY.ROW3 -> /lhs/LHS Keys/KEY.ROW9
- D49 pad 3: /lhs/LHS Keys/KEY.ROW4 -> /lhs/LHS Keys/KEY.ROW10
- D49 pad 6: /lhs/LHS Keys/KEY.ROW4 -> /lhs/LHS Keys/KEY.ROW10
- D49 pad 7: /lhs/LHS Keys/KEY.ROW4 -> /lhs/LHS Keys/KEY.ROW10
- D49 pad 8: /lhs/LHS Keys/KEY.ROW4 -> /lhs/LHS Keys/KEY.ROW10
- D7 pad 3: /rhs/RHS Keys/KEY.ROW2 -> /rhs/RHS Keys/KEY.ROW4
- D7 pad 6: /rhs/RHS Keys/KEY.ROW2 -> /rhs/RHS Keys/KEY.ROW4
- D7 pad 7: /rhs/RHS Keys/KEY.ROW2 -> /rhs/RHS Keys/KEY.ROW4
- D7 pad 8: /rhs/RHS Keys/KEY.ROW2 -> /rhs/RHS Keys/KEY.ROW4
- D8 pad 3: /rhs/RHS Keys/KEY.ROW1 -> /rhs/RHS Keys/KEY.ROW3
- D8 pad 6: /rhs/RHS Keys/KEY.ROW1 -> /rhs/RHS Keys/KEY.ROW3
- D8 pad 7: /rhs/RHS Keys/KEY.ROW1 -> /rhs/RHS Keys/KEY.ROW3
- D8 pad 8: /rhs/RHS Keys/KEY.ROW1 -> /rhs/RHS Keys/KEY.ROW3
- D80 pad 1: /lhs/LHS LEDs/LED.CS_COL10 -> /lhs/LHS LEDs/LED.CS_COL11
- U5 pad 1: /lhs/LHS LEDs/LED.CS_COL8 -> /lhs/LHS Keys/KEY.COL2
- U5 pad 10: /lhs/LHS LEDs/LED.CS_COL10 -> /lhs/LHS LEDs/LED.CS_COL3
- U5 pad 11: /lhs/LHS LEDs/LED.CS_COL11 -> /lhs/LHS LEDs/LED.CS_COL5
- U5 pad 12: /lhs/LHS LEDs/LED.CS_COL12 -> /lhs/LHS LEDs/LED.CS_COL7
- U5 pad 13: /lhs/LHS LEDs/LED.CS_COL13 -> /lhs/LHS LEDs/LED.CS_COL9
- U5 pad 14: /lhs/LHS LEDs/LED.CS_COL14 -> /lhs/LHS LEDs/LED.CS_COL11
- U5 pad 15: /lhs/LHS LEDs/LED.CS_COL15 -> /lhs/LHS LEDs/LED.CS_COL13
- U5 pad 16: /lhs/LHS LEDs/LED.CS_COL16 -> /lhs/LHS LEDs/LED.CS_COL15
- U5 pad 17: /lhs/LHS LEDs/LED.SW_GREEN4 -> /lhs/LHS LEDs/LED.SW_BLUE3
- U5 pad 18: /lhs/LHS LEDs/LED.SW_RED4 -> /lhs/LHS LEDs/LED.SW_GREEN3
- U5 pad 19: /lhs/LHS LEDs/LED.SW_BLUE4 -> /lhs/LHS LEDs/LED.SW_RED4
- U5 pad 2: /lhs/LHS LEDs/LED.CS_COL7 -> /lhs/LHS Keys/KEY.COL4
- U5 pad 20: /lhs/LHS LEDs/LED.SW_GREEN3 -> /lhs/LHS Keys/KEY.ROW6
- U5 pad 21: /lhs/LHS LEDs/LED.SW_RED3 -> /lhs/LHS Keys/KEY.ROW8
- U5 pad 22: /lhs/LHS LEDs/LED.SW_BLUE3 -> /lhs/LHS Keys/KEY.ROW10
- U5 pad 23: /lhs/LHS LEDs/LED.SW_GREEN2 -> /lhs/LHS Keys/KEY.COL7
- U5 pad 24: /lhs/LHS LEDs/LED.SW_RED2 -> /lhs/LHS Keys/KEY.COL9
- U5 pad 25: /lhs/LHS LEDs/LED.SW_BLUE2 -> /lhs/LHS Keys/KEY.COL10
- U5 pad 26: /lhs/LHS LEDs/LED.SW_GREEN1 -> /lhs/LHS Keys/KEY.COL8
- U5 pad 27: /lhs/LHS LEDs/LED.SW_RED1 -> /lhs/LHS Keys/KEY.COL6
- U5 pad 28: /lhs/LHS LEDs/LED.SW_BLUE1 -> /lhs/LHS Keys/KEY.ROW9
- U5 pad 3: /lhs/LHS LEDs/LED.CS_COL6 -> /lhs/LHS Keys/KEY.ROW5
- U5 pad 30: /lhs/LHS Keys/KEY.ROW6 -> /lhs/LHS LEDs/LED.SW_BLUE4
- U5 pad 31: /lhs/LHS Keys/KEY.ROW5 -> /lhs/LHS LEDs/LED.SW_GREEN4
- U5 pad 32: /lhs/LHS Keys/KEY.ROW4 -> /lhs/LHS LEDs/LED.SW_RED3
- U5 pad 33: /lhs/LHS Keys/KEY.ROW3 -> /lhs/LHS LEDs/LED.CS_COL16
- U5 pad 34: /lhs/LHS Keys/KEY.ROW2 -> /lhs/LHS LEDs/LED.CS_COL14
- U5 pad 35: /lhs/LHS Keys/KEY.ROW1 -> /lhs/LHS LEDs/LED.CS_COL12
- U5 pad 36: /lhs/LHS Keys/KEY.COL1 -> /lhs/LHS LEDs/LED.CS_COL10
- U5 pad 37: /lhs/LHS Keys/KEY.COL2 -> /lhs/LHS LEDs/LED.CS_COL8
- U5 pad 38: /lhs/LHS Keys/KEY.COL3 -> /lhs/LHS LEDs/LED.CS_COL6
- U5 pad 39: /lhs/LHS Keys/KEY.COL4 -> /lhs/LHS LEDs/LED.CS_COL4
- U5 pad 4: /lhs/LHS LEDs/LED.CS_COL5 -> /lhs/LHS Keys/KEY.ROW3
- U5 pad 40: /lhs/LHS Keys/KEY.COL5 -> /lhs/LHS LEDs/LED.CS_COL2
- U5 pad 41: /lhs/LHS Keys/KEY.COL6 -> /lhs/LHS LEDs/LED.SW_RED2
- U5 pad 42: /lhs/LHS Keys/KEY.COL7 -> /lhs/LHS LEDs/LED.SW_GREEN1
- U5 pad 43: /lhs/LHS Keys/KEY.COL8 -> /lhs/LHS LEDs/LED.SW_BLUE1
- U5 pad 44: /lhs/LHS Keys/KEY.COL9 -> /lhs/LHS Keys/KEY.ROW2
- U5 pad 45: /lhs/LHS Keys/KEY.COL10 -> /lhs/LHS Keys/KEY.ROW4
- U5 pad 46: (no net) -> /lhs/LHS Keys/KEY.COL5
- U5 pad 47: (no net) -> /lhs/LHS Keys/KEY.COL3
- U5 pad 48: /lhs/LHS Keys/KEY.ROW10 -> /lhs/LHS Keys/KEY.COL1
- U5 pad 5: /lhs/LHS LEDs/LED.CS_COL4 -> /lhs/LHS Keys/KEY.ROW1
- U5 pad 6: /lhs/LHS LEDs/LED.CS_COL3 -> /lhs/LHS LEDs/LED.SW_RED1
- U5 pad 7: /lhs/LHS LEDs/LED.CS_COL2 -> /lhs/LHS LEDs/LED.SW_GREEN2
- U5 pad 8: /lhs/LHS LEDs/LED.CS_COL1 -> /lhs/LHS LEDs/LED.SW_BLUE2
- U5 pad 9: /lhs/LHS LEDs/LED.CS_COL9 -> /lhs/LHS LEDs/LED.CS_COL1
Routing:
- net /rhs/RHS Keys/KEY.ROW2: track 167.9 -> 0.00 mm, vias 1 -> 0
- net /lhs/LHS Keys/KEY.ROW4: track 153.0 -> 0.00 mm, vias 3 -> 0
- net /lhs/LHS LEDs/LED.CS_COL11: track 46.9 -> 199.0 mm, vias 3 -> 4
- net /lhs/LHS Keys/KEY.ROW9: track 0.00 -> 128.4 mm, vias 0 -> 2
- net /rhs/RHS Keys/KEY.ROW4: track 0.00 -> 126.7 mm, vias 0 -> 2
- net /lhs/LHS Keys/KEY.ROW3: track 121.4 -> 0.00 mm, vias 2 -> 0
- net /lhs/LHS Keys/KEY.COL1: track 47.5 -> 165.9 mm, vias 1 -> 0
- net /rhs/RHS Keys/KEY.ROW1: track 114.7 -> 0.00 mm
- net /lhs/LHS Keys/KEY.COL2: track 55.7 -> 165.3 mm
- net /lhs/LHS Keys/KEY.ROW10: track 0.00 -> 103.2 mm
- net /rhs/RHS Keys/KEY.ROW3: track 0.00 -> 103.1 mm
- net /lhs/LHS LEDs/LED.CS_COL2: track 74.3 -> 176.6 mm, vias 2 -> 1
- net /lhs/LHS LEDs/LED.CS_COL3: track 80.8 -> 181.3 mm, vias 0 -> 1
- net /lhs/LHS LEDs/LED.CS_COL1: track 77.6 -> 166.3 mm, vias 2 -> 1
- net /lhs/LHS Keys/KEY.COL7: track 166.1 -> 83.5 mm
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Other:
- board size 156.2 x 227.5 mm -> 304 x 221 mm

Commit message: Update schematics to match new footprints
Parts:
- added J4: USB_C_Receptacle_USB2.0, Nour_KB:GCT_USB4085-GF-A_REVA4, F.Cu at (28.0, 59.0)
- added J5: SJ-435107RS, Nour_KB:CUI_SJ-435107RS, F.Cu at (9.25, 55.0)
- moved J3 79.2 mm to (28.0, 2.25)
- moved J1 42.4 mm to (9.25, 6.00)
- moved U4 35.7 mm to (20.2, 28.0)
- moved C14 3.72 mm to (33.2, -4.25)
- moved R1 2.89 mm to (96.1, 2.75)
- moved R3 2.11 mm to (96.1, 9.00)
- moved R5 1.09 mm to (93.2, -0.41)
- moved R12 0.54 mm to (54.3, -8.25)
- moved IC1 0.40 mm to (43.2, -8.50)
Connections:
- U4 pad 1: /core/LED.CS_COL8 -> /core/KEY.COL2
- U4 pad 10: /core/LED.CS_COL10 -> /core/LED.CS_COL3
- U4 pad 11: /core/LED.CS_COL11 -> /core/LED.CS_COL5
- U4 pad 12: /core/LED.CS_COL12 -> /core/LED.CS_COL7
- U4 pad 13: /core/LED.CS_COL13 -> /core/LED.CS_COL9
- U4 pad 14: /core/LED.CS_COL14 -> /core/LED.CS_COL11
- U4 pad 15: /core/LED.CS_COL15 -> /core/LED.CS_COL13
- U4 pad 16: /core/LED.CS_COL16 -> /core/LED.CS_COL15
- U4 pad 17: /core/LED.SW_GREEN4 -> /core/LED.SW_BLUE3
- U4 pad 18: /core/LED.SW_RED4 -> /core/LED.SW_GREEN3
- U4 pad 19: /core/LED.SW_BLUE4 -> /core/LED.SW_RED4
- U4 pad 2: /core/LED.CS_COL7 -> /core/KEY.COL4
- U4 pad 20: /core/LED.SW_GREEN3 -> /core/KEY.ROW6
- U4 pad 21: /core/LED.SW_RED3 -> /core/KEY.ROW8
- U4 pad 22: /core/LED.SW_BLUE3 -> /core/KEY.ROW10
- U4 pad 23: /core/LED.SW_GREEN2 -> /core/KEY.COL7
- U4 pad 24: /core/LED.SW_RED2 -> /core/KEY.COL9
- U4 pad 25: /core/LED.SW_BLUE2 -> /core/KEY.COL10
- U4 pad 26: /core/LED.SW_GREEN1 -> /core/KEY.COL8
- U4 pad 27: /core/LED.SW_RED1 -> /core/KEY.COL6
- U4 pad 28: /core/LED.SW_BLUE1 -> /core/KEY.ROW9
- U4 pad 3: /core/LED.CS_COL6 -> /core/KEY.ROW5
- U4 pad 30: /core/KEY.ROW6 -> /core/LED.SW_BLUE4
- U4 pad 31: /core/KEY.ROW5 -> /core/LED.SW_GREEN4
- U4 pad 32: /core/KEY.ROW4 -> /core/LED.SW_RED3
- U4 pad 33: /core/KEY.ROW3 -> /core/LED.CS_COL16
- U4 pad 34: /core/KEY.ROW2 -> /core/LED.CS_COL14
- U4 pad 35: /core/KEY.ROW1 -> /core/LED.CS_COL12
- U4 pad 36: /core/KEY.COL1 -> /core/LED.CS_COL10
- U4 pad 37: /core/KEY.COL2 -> /core/LED.CS_COL8
- U4 pad 38: /core/KEY.COL3 -> /core/LED.CS_COL6
- U4 pad 39: /core/KEY.COL4 -> /core/LED.CS_COL4
- U4 pad 4: /core/LED.CS_COL5 -> /core/KEY.ROW3
- U4 pad 40: /core/KEY.COL5 -> /core/LED.CS_COL2
- U4 pad 41: /core/KEY.COL6 -> /core/LED.SW_RED2
- U4 pad 42: /core/KEY.COL7 -> /core/LED.SW_GREEN1
- U4 pad 43: /core/KEY.COL8 -> /core/LED.SW_BLUE1
- U4 pad 44: /core/KEY.COL9 -> /core/KEY.ROW2
- U4 pad 45: /core/KEY.COL10 -> /core/KEY.ROW4
- U4 pad 46: (no net) -> /core/KEY.COL5
- U4 pad 47: (no net) -> /core/KEY.COL3
- U4 pad 48: /core/KEY.ROW10 -> /core/KEY.COL1
- U4 pad 5: /core/LED.CS_COL4 -> /core/KEY.ROW1
- U4 pad 6: /core/LED.CS_COL3 -> /core/LED.SW_RED1
- U4 pad 7: /core/LED.CS_COL2 -> /core/LED.SW_GREEN2
- U4 pad 8: /core/LED.CS_COL1 -> /core/LED.SW_BLUE2
- U4 pad 9: /core/LED.CS_COL9 -> /core/LED.CS_COL1
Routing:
- net /lhs/LHS Keys/KEY.ROW2: track 126.3 -> 128.2 mm
- removed copper zone on B.Cu, net GND
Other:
- board size 304 x 221 mm -> 304 x 240 mm

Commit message: Deal with DRC warnings due to silkscreen clipped by solder mask
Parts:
- moved J4 0.10 mm to (28.0, 58.9)
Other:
- outline, holes or cut-outs redrawn
